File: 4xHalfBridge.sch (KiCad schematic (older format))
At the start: 53 parts, among them U2 VSON8_Nexfet, U3 VSON8_Nexfet, U4 VSON8_Nexfet, U5 VSON8_Nexfet, U6 VSON8_Nexfet, U7 VSON8_Nexfet, U8 VSON8_Nexfet, U9 VSON8_Nexfet

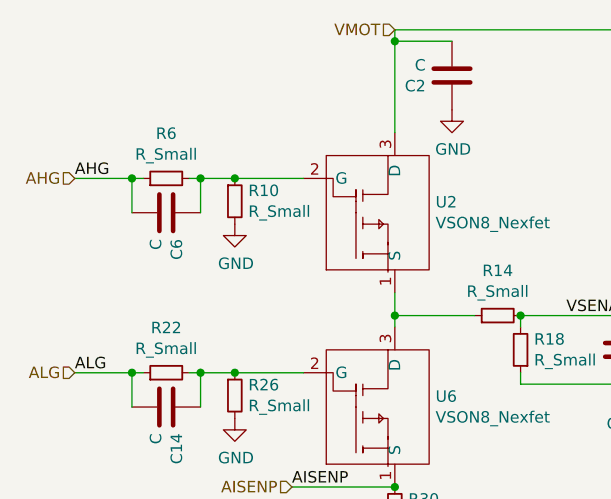
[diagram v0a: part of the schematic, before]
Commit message: update passive components values
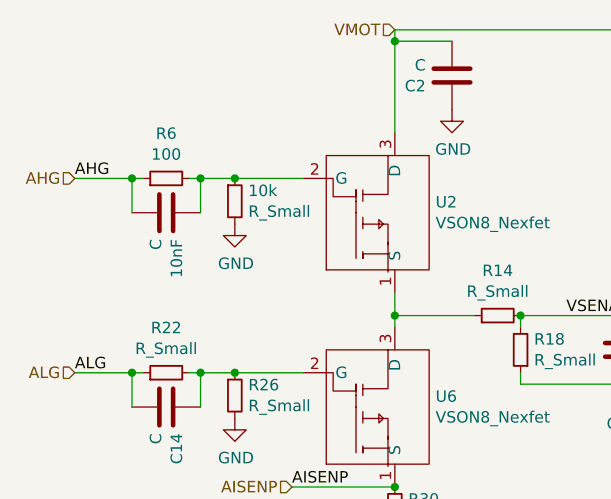
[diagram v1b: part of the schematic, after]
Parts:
- R6: value R_Small -> 100
- renumbered R10 to 10k, C6 to 10nF
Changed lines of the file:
@@
 P 1100 1700
 AR Path="/612B3EC1" Ref="C?"  Part="1"
-AR Path="/6121F53E/612B3EC1" Ref="C6"  Part="1"
-F 0 "C6" H 985 1654 50  0000 R CNN
+AR Path="/6121F53E/612B3EC1" Ref="10nF"  Part="1"
+F 0 "10nF" H 985 1654 50  0000 R CNN
 F 1 "C" H 985 1745 50  0000 R CNN
 F 2 "Capacitor_SMD:C_0402_1005Metric" H 1138 1550 50  0001 C CNN
@@
 P 1100 1550
 F 0 "R6" V 1296 1550 50  0000 C CNN
-F 1 "R_Small" V 1205 1550 50  0000 C CNN
+F 1 "100" V 1205 1550 50  0000 C CNN
 F 2 "Resistor_SMD:R_0603_1608Metric" H 1100 1550 50  0001 C CNN
 F 3 "~" H 1100 1550 50  0001 C CNN
@@
 Connection ~ 5250 2150
 $Comp
-L Device:R_Small R10
+L Device:R_Small 10k
 U 1 1 614B666E
 P 1400 1650
-F 0 "R10" H 1459 1696 50  0000 L CNN
+F 0 "10k" H 1459 1696 50  0000 L CNN
 F 1 "R_Small" H 1459 1605 50  0000 L CNN
 F 2 "Resistor_SMD:R_0603_1608Metric" H 1400 1650 50  0001 C CNN
